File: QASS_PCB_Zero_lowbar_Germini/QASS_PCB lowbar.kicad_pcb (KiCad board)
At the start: 2 copper layers, 219.1 x 110.5 mm, 108 parts, among them J2 Conn_01x05_Pin, J3 Conn_01x05_Pin, J4 Conn_01x02_Pin, J5 Conn_01x05_Pin, J6 Conn_01x05_Pin, U2 RP2040-Matrix

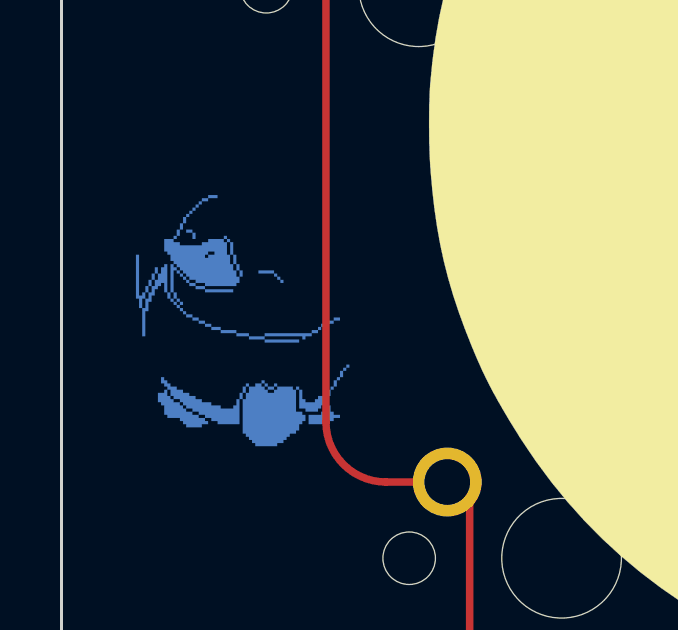
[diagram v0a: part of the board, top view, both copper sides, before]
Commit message: PCB lowbar for Gemini finished. Ordered. Untested yet.
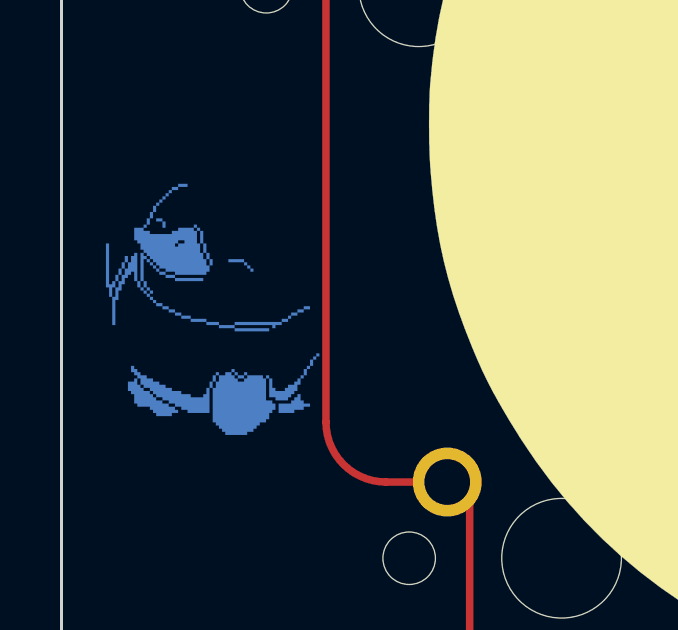
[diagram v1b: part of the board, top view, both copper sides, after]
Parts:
- removed the REF** at (30.0, 59.3)
- added REF**: Clacktales_9mm_whiteSilk, Silkscreen:Clacktales_9mm_whiteSilk, B.Cu at (29.0, 59.0)
- moved Ref** 1.32 mm to (29.5, 70.3)
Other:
- board text added: "Backup-Switch pins for long spacebar"
- board text added: "Re-fork of fork by quark-works: https://github.com/quark-works/QASS-Zero"
- board text removed: "Switch pins for long spacebars"
- board text removed: "Zero by quark-works: https://github.com/quark-works/QASS-Zero"
